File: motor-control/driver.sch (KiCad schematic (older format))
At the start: 24 parts

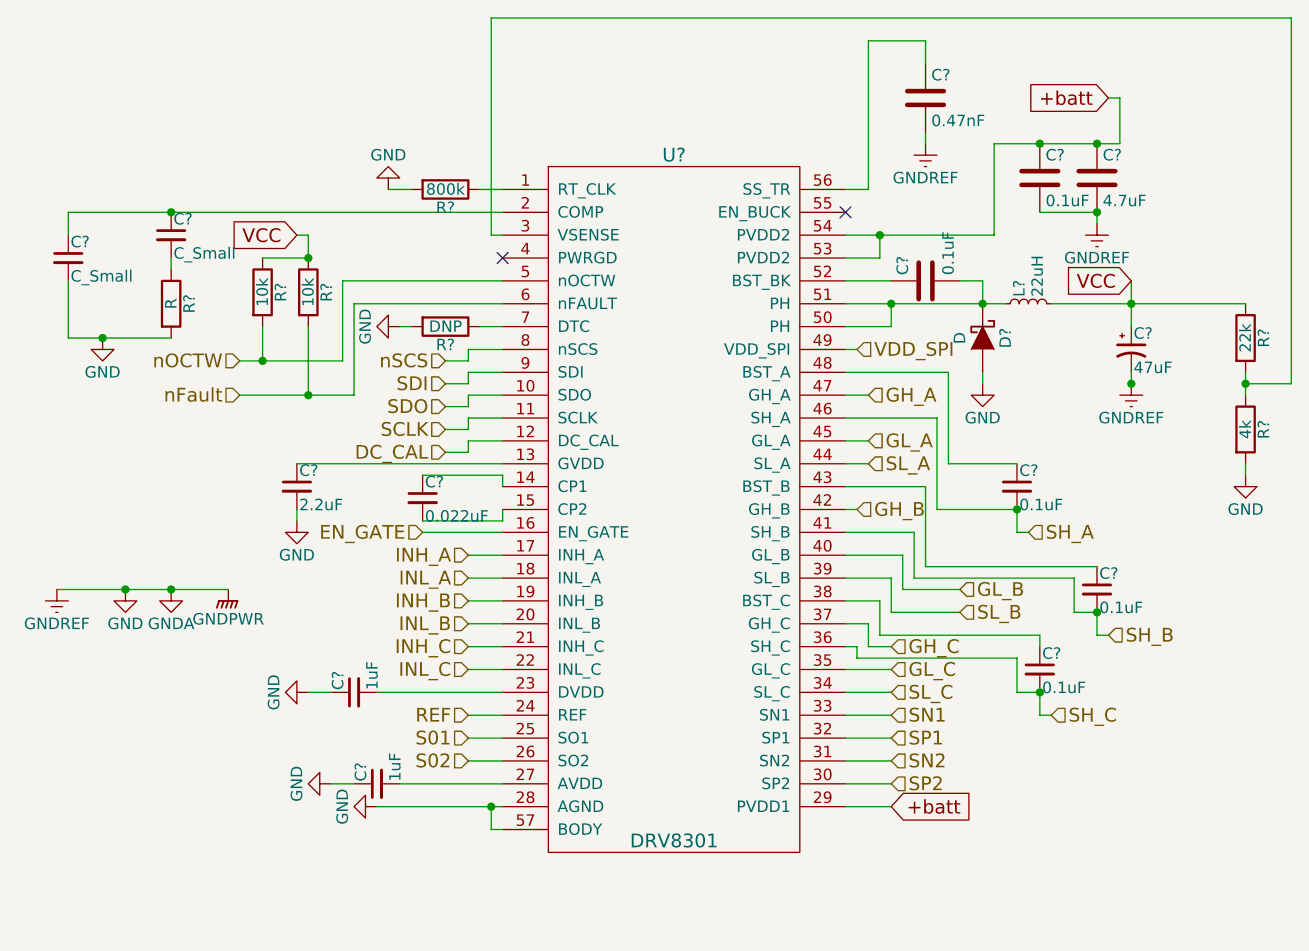
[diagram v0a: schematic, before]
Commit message: Annotated schematic & matched footprints
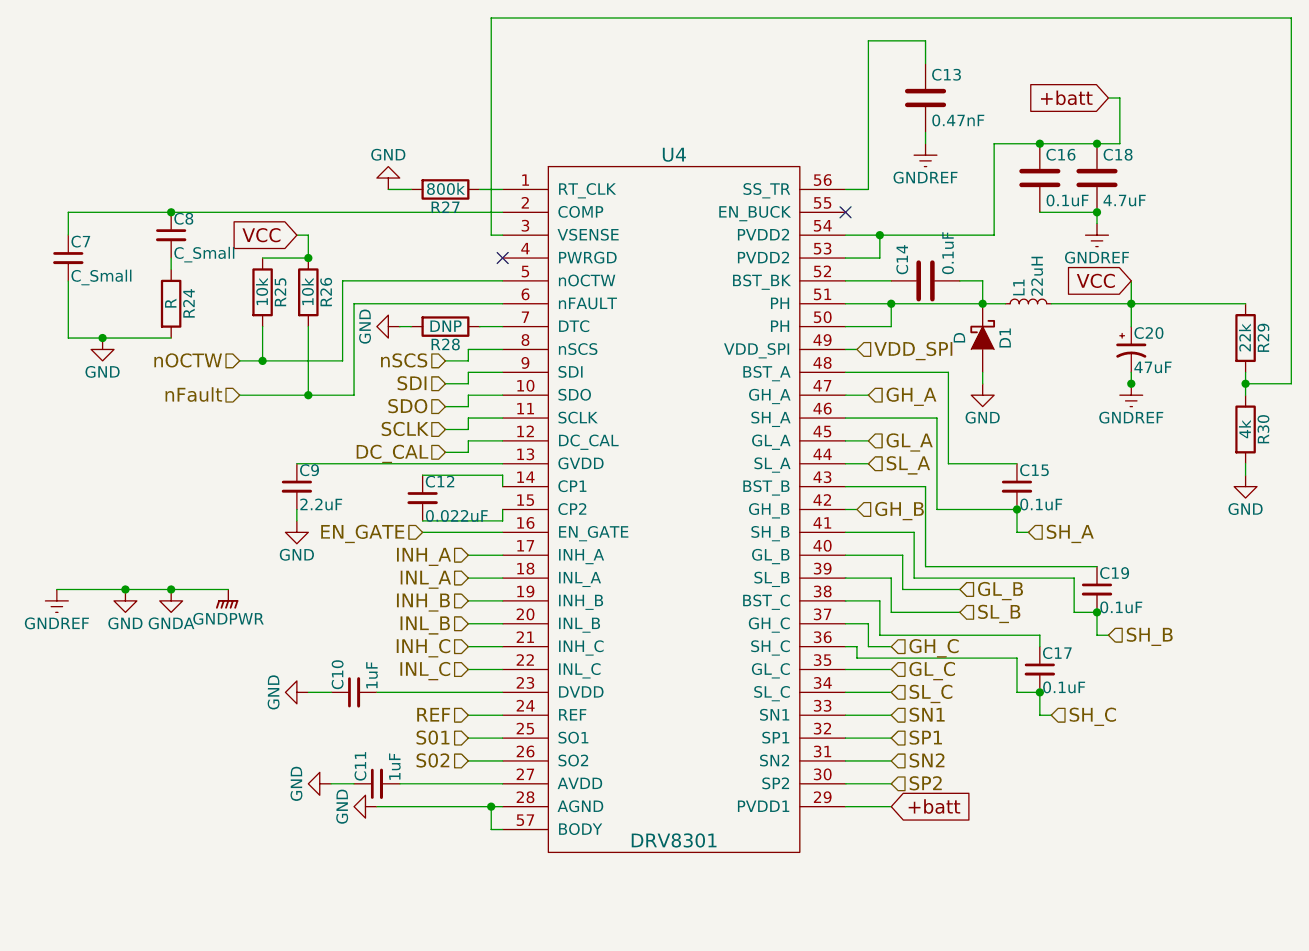
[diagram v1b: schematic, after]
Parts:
- C10, C11, C12, C13, C14, C15, C17, C19, C7, C8, C9: renamed from C?; footprint (none) -> Capacitors_SMD:C_0805
- C16: renamed from C?; footprint (none) -> Capacitors_Elko_ThroughHole:Elko_vert_31.5x14mm_RM5
- C18, C20: renamed from C?; footprint (none) -> Capacitors_Elko_ThroughHole:Elko_vert_31.5x16mm_RM7.5
- D1: renamed from D?; footprint (none) -> Capacitors_SMD:C_0805
- L1: renamed from L?; footprint (none) -> Capacitors_SMD:C_0805
- R24, R25, R26, R27, R28, R29, R30: renamed from R?; footprint (none) -> Resistors_SMD:R_0805
- U4: renamed from U?; footprint (none) -> p16261:DRV8301

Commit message: Just trying to get things together
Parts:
- C16: footprint Capacitors_Elko_ThroughHole:Elko_vert_31.5x14mm_RM5 -> Capacitors_SMD:C_0805
- C18, C20: footprint Capacitors_Elko_ThroughHole:Elko_vert_31.5x16mm_RM7.5 -> Capacitors_SMD:C_0805
- D1: footprint Capacitors_SMD:C_0805 -> Diodes_ThroughHole:Diode_TO-247_Vertical
- L1: footprint Capacitors_SMD:C_0805 -> Inductors:INDUCTOR_V
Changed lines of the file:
@@
 F 0 "C16" H 6525 2000 50  0000 L CNN
 F 1 "0.1uF" H 6525 1800 50  0000 L CNN
-F 2 "Capacitors_Elko_ThroughHole:Elko_vert_31.5x14mm_RM5" H 6538 1750 30  0001 C CNN
+F 2 "Capacitors_SMD:C_0805" H 6538 1750 30  0001 C CNN
 F 3 "" H 6500 1900 60  0000 C CNN
 	1    6500 1900
@@
 F 0 "C18" H 6775 2000 50  0000 L CNN
 F 1 "4.7uF" H 6775 1800 50  0000 L CNN
-F 2 "Capacitors_Elko_ThroughHole:Elko_vert_31.5x16mm_RM7.5" H 6788 1750 30  0001 C CNN
+F 2 "Capacitors_SMD:C_0805" H 6788 1750 30  0001 C CNN
 F 3 "" H 6750 1900 60  0000 C CNN
 	1    6750 1900
@@
 F 0 "L1" H 6480 2490 50  0000 L CNN
 F 1 "22uH" H 6480 2410 50  0000 L CNN
-F 2 "Capacitors_SMD:C_0805" H 6450 2450 60  0001 C CNN
+F 2 "Inductors:INDUCTOR_V" H 6450 2450 60  0001 C CNN
 F 3 "" H 6450 2450 60  0000 C CNN
 	1    6450 2450
@@
 F 0 "D1" H 6250 2700 50  0000 C CNN
 F 1 "D" H 6250 2500 50  0000 C CNN
-F 2 "Capacitors_SMD:C_0805" H 6250 2600 60  0001 C CNN
+F 2 "Diodes_ThroughHole:Diode_TO-247_Vertical" H 6250 2600 60  0001 C CNN
 F 3 "" H 6250 2600 60  0000 C CNN
 	1    6250 2600
@@
 F 0 "C20" H 6910 2720 50  0000 L CNN
 F 1 "47uF" H 6910 2570 50  0000 L CNN
-F 2 "Capacitors_Elko_ThroughHole:Elko_vert_31.5x16mm_RM7.5" H 6900 2650 60  0001 C CNN
+F 2 "Capacitors_SMD:C_0805" H 6900 2650 60  0001 C CNN
 F 3 "" H 6900 2650 60  0000 C CNN
 	1    6900 2650

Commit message: More changes
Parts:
- added C21: C_Small, symbol C_Small
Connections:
- net +batt: now also C21.1
- net GND: now also C21.2
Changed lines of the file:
@@
 $EndComp
 $Comp
-L GNDREF #PWR31
+L GNDREF #PWR32
 U 1 1 56449729
 P 6000 1750
-F 0 "#PWR31" H 6000 1500 50  0001 C CNN
+F 0 "#PWR32" H 6000 1500 50  0001 C CNN
 F 1 "GNDREF" H 6000 1600 50  0000 C CNN
 F 2 "" H 6000 1750 60  0000 C CNN
@@
 $EndComp
 $Comp
-L GNDREF #PWR33
+L GNDREF #PWR34
 U 1 1 5644A61D
 P 6750 2100
-F 0 "#PWR33" H 6750 1850 50  0001 C CNN
+F 0 "#PWR34" H 6750 1850 50  0001 C CNN
 F 1 "GNDREF" H 6750 1950 50  0000 C CNN
 F 2 "" H 6750 2100 60  0000 C CNN
@@
 VCC
 $Comp
-L GNDREF #PWR34
+L GNDREF #PWR35
 U 1 1 5644A955
 P 6900 2800
-F 0 "#PWR34" H 6900 2550 50  0001 C CNN
+F 0 "#PWR35" H 6900 2550 50  0001 C CNN
 F 1 "GNDREF" H 6900 2650 50  0000 C CNN
 F 2 "" H 6900 2800 60  0000 C CNN
@@
 	7400 2750 7400 2850
 $Comp
-L GND #PWR35
+L GND #PWR36
 U 1 1 56511C27
 P 7400 3200
-F 0 "#PWR35" H 7400 2950 50  0001 C CNN
+F 0 "#PWR36" H 7400 2950 50  0001 C CNN
 F 1 "GND" H 7400 3050 50  0000 C CNN
 F 2 "" H 7400 3200 60  0000 C CNN
@@
 Connection ~ 7400 2800
 $Comp
-L GND #PWR32
+L GND #PWR33
 U 1 1 56512446
 P 6250 2800
-F 0 "#PWR32" H 6250 2550 50  0001 C CNN
+F 0 "#PWR33" H 6250 2550 50  0001 C CNN
 F 1 "GND" H 6250 2650 50  0000 C CNN
 F 2 "" H 6250 2800 60  0000 C CNN
@@
 Connection ~ 2500 3700
 Connection ~ 2700 3700
+$Comp
+L C_Small C21
+U 1 1 56914993
+P 5700 4800
+F 0 "C21" H 5710 4870 50  0000 L CNN
+F 1 "C_Small" H 5710 4720 50  0000 L CNN
+F 2 "" H 5700 4800 50  0000 C CNN
+F 3 "" H 5700 4800 50  0000 C CNN
+	1    5700 4800
+	1    0    0    -1
+$EndComp
+$Comp
+L GND #PWR31
+U 1 1 56914B46
+P 5700 5000
+F 0 "#PWR31" H 5700 4750 50  0001 C CNN
+F 1 "GND" H 5700 4850 50  0000 C CNN
+F 2 "" H 5700 5000 50  0000 C CNN
+F 3 "" H 5700 5000 50  0000 C CNN
+	1    5700 5000
+	1    0    0    -1
+$EndComp
+Wire Wire Line
+	5700 4900 5700 5000
+Wire Wire Line
+	5700 4700 5700 4650
+Connection ~ 5700 4650
 $EndSCHEMATC

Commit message: Stuff I didn't commit from last time
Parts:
- C21: footprint (none) -> Capacitors_SMD:C_0805
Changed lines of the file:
@@
 $EndComp
 $Comp
-L GNDREF #PWR32
+L GNDREF #PWR020
 U 1 1 56449729
 P 6000 1750
-F 0 "#PWR32" H 6000 1500 50  0001 C CNN
+F 0 "#PWR020" H 6000 1500 50  0001 C CNN
 F 1 "GNDREF" H 6000 1600 50  0000 C CNN
 F 2 "" H 6000 1750 60  0000 C CNN
@@
 $EndComp
 $Comp
-L GNDREF #PWR34
+L GNDREF #PWR021
 U 1 1 5644A61D
 P 6750 2100
-F 0 "#PWR34" H 6750 1850 50  0001 C CNN
+F 0 "#PWR021" H 6750 1850 50  0001 C CNN
 F 1 "GNDREF" H 6750 1950 50  0000 C CNN
 F 2 "" H 6750 2100 60  0000 C CNN
@@
 VCC
 $Comp
-L GNDREF #PWR35
+L GNDREF #PWR022
 U 1 1 5644A955
 P 6900 2800
-F 0 "#PWR35" H 6900 2550 50  0001 C CNN
+F 0 "#PWR022" H 6900 2550 50  0001 C CNN
 F 1 "GNDREF" H 6900 2650 50  0000 C CNN
 F 2 "" H 6900 2800 60  0000 C CNN
@@
 $EndComp
 $Comp
-L GND #PWR29
+L GND #PWR023
 U 1 1 5650F368
 P 3650 1950
-F 0 "#PWR29" H 3650 1700 50  0001 C CNN
+F 0 "#PWR023" H 3650 1700 50  0001 C CNN
 F 1 "GND" H 3650 1800 50  0000 C CNN
 F 2 "" H 3650 1950 60  0000 C CNN
@@
 	2250 2600 2700 2600
 $Comp
-L GND #PWR21
+L GND #PWR024
 U 1 1 5650F526
 P 2400 2600
-F 0 "#PWR21" H 2400 2350 50  0001 C CNN
+F 0 "#PWR024" H 2400 2350 50  0001 C CNN
 F 1 "GND" H 2400 2450 50  0000 C CNN
 F 2 "" H 2400 2600 60  0000 C CNN
@@
 $EndComp
 $Comp
-L GND #PWR26
+L GND #PWR025
 U 1 1 5650F58D
 P 3300 4150
-F 0 "#PWR26" H 3300 3900 50  0001 C CNN
+F 0 "#PWR025" H 3300 3900 50  0001 C CNN
 F 1 "GND" H 3300 4000 50  0000 C CNN
 F 2 "" H 3300 4150 60  0000 C CNN
@@
 $EndComp
 $Comp
-L GND #PWR27
+L GND #PWR026
 U 1 1 5650FDA1
 P 3400 4550
-F 0 "#PWR27" H 3400 4300 50  0001 C CNN
+F 0 "#PWR026" H 3400 4300 50  0001 C CNN
 F 1 "GND" H 3400 4400 50  0000 C CNN
 F 2 "" H 3400 4550 60  0000 C CNN
@@
 	3700 4550 4150 4550
 $Comp
-L GND #PWR28
+L GND #PWR027
 U 1 1 5650FE56
 P 3600 4650
-F 0 "#PWR28" H 3600 4400 50  0001 C CNN
+F 0 "#PWR027" H 3600 4400 50  0001 C CNN
 F 1 "GND" H 3600 4500 50  0000 C CNN
 F 2 "" H 3600 4650 60  0000 C CNN
@@
 	7400 2750 7400 2850
 $Comp
-L GND #PWR36
+L GND #PWR028
 U 1 1 56511C27
 P 7400 3200
-F 0 "#PWR36" H 7400 2950 50  0001 C CNN
+F 0 "#PWR028" H 7400 2950 50  0001 C CNN
 F 1 "GND" H 7400 3050 50  0000 C CNN
 F 2 "" H 7400 3200 60  0000 C CNN
@@
 Connection ~ 7400 2800
 $Comp
-L GND #PWR33
+L GND #PWR029
 U 1 1 56512446
 P 6250 2800
-F 0 "#PWR33" H 6250 2550 50  0001 C CNN
+F 0 "#PWR029" H 6250 2550 50  0001 C CNN
 F 1 "GND" H 6250 2650 50  0000 C CNN
 F 2 "" H 6250 2800 60  0000 C CNN
@@
 $EndComp
 $Comp
-L GND #PWR30
+L GND #PWR030
 U 1 1 56513ADE
 P 3700 2550
-F 0 "#PWR30" H 3700 2300 50  0001 C CNN
+F 0 "#PWR030" H 3700 2300 50  0001 C CNN
 F 1 "GND" H 3700 2400 50  0000 C CNN
 F 2 "" H 3700 2550 60  0000 C CNN
@@
 	4000 3050 4150 3050
 $Comp
-L GND #PWR25
+L GND #PWR031
 U 1 1 565164C8
 P 3250 3400
-F 0 "#PWR25" H 3250 3150 50  0001 C CNN
+F 0 "#PWR031" H 3250 3150 50  0001 C CNN
 F 1 "GND" H 3250 3250 50  0000 C CNN
 F 2 "" H 3250 3400 60  0000 C CNN
@@
 	5650 4250 5850 4250
 $Comp
-L GND #PWR22
+L GND #PWR032
 U 1 1 5651CA8A
 P 2500 3700
-F 0 "#PWR22" H 2500 3450 50  0001 C CNN
+F 0 "#PWR032" H 2500 3450 50  0001 C CNN
 F 1 "GND" H 2500 3550 50  0000 C CNN
 F 2 "" H 2500 3700 60  0000 C CNN
@@
 $EndComp
 $Comp
-L GNDA #PWR23
+L GNDA #PWR033
 U 1 1 5651CACE
 P 2700 3700
-F 0 "#PWR23" H 2700 3450 50  0001 C CNN
+F 0 "#PWR033" H 2700 3450 50  0001 C CNN
 F 1 "GNDA" H 2700 3550 50  0000 C CNN
 F 2 "" H 2700 3700 60  0000 C CNN
@@
 $EndComp
 $Comp
-L GNDPWR #PWR24
+L GNDPWR #PWR034
 U 1 1 5651CB12
 P 2950 3700
-F 0 "#PWR24" H 2950 3500 50  0001 C CNN
+F 0 "#PWR034" H 2950 3500 50  0001 C CNN
 F 1 "GNDPWR" H 2950 3570 50  0000 C CNN
 F 2 "" H 2950 3650 60  0000 C CNN
@@
 $EndComp
 $Comp
-L GNDREF #PWR20
+L GNDREF #PWR035
 U 1 1 5651CB56
 P 2200 3700
-F 0 "#PWR20" H 2200 3450 50  0001 C CNN
+F 0 "#PWR035" H 2200 3450 50  0001 C CNN
 F 1 "GNDREF" H 2200 3550 50  0000 C CNN
 F 2 "" H 2200 3700 60  0000 C CNN
@@
 F 0 "C21" H 5710 4870 50  0000 L CNN
 F 1 "C_Small" H 5710 4720 50  0000 L CNN
-F 2 "" H 5700 4800 50  0000 C CNN
+F 2 "Capacitors_SMD:C_0805" H 5700 4800 50  0001 C CNN
 F 3 "" H 5700 4800 50  0000 C CNN
 	1    5700 4800
@@
 $EndComp
 $Comp
-L GND #PWR31
+L GND #PWR036
 U 1 1 56914B46
 P 5700 5000
-F 0 "#PWR31" H 5700 4750 50  0001 C CNN
+F 0 "#PWR036" H 5700 4750 50  0001 C CNN
 F 1 "GND" H 5700 4850 50  0000 C CNN
 F 2 "" H 5700 5000 50  0000 C CNN

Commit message: Modified Schematic Comp resist/cap vals, added bom
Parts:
- R28: value DNP -> 0R
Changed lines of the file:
@@
 P 3900 2550
 F 0 "R28" V 3980 2550 50  0000 C CNN
-F 1 "DNP" V 3900 2550 50  0000 C CNN
+F 1 "0R" V 3900 2550 50  0000 C CNN
 F 2 "Resistors_SMD:R_0805" V 3830 2550 30  0001 C CNN
 F 3 "" H 3900 2550 30  0000 C CNN

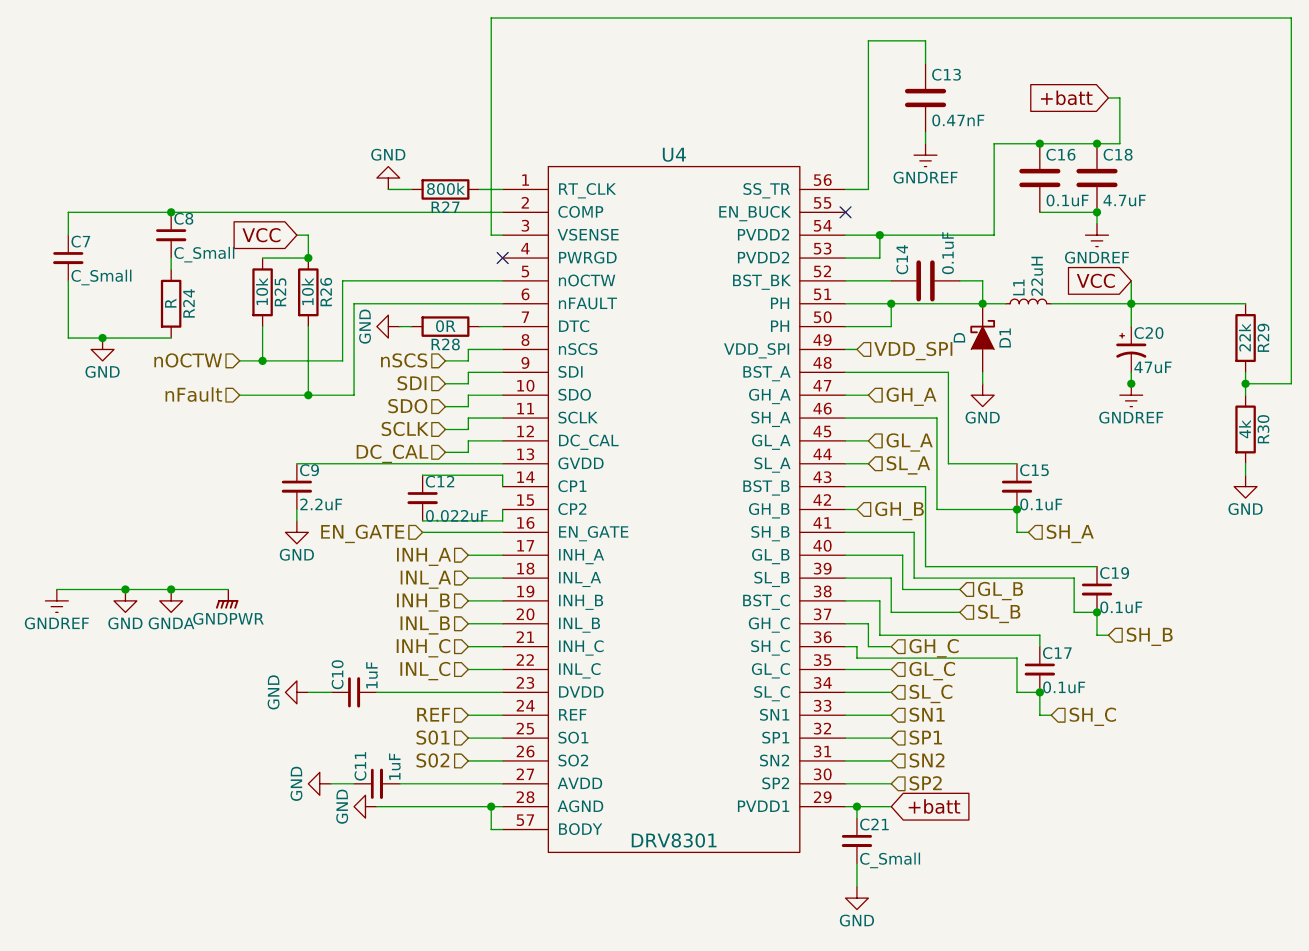
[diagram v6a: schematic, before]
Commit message: Added some datasheet links, additional RC values
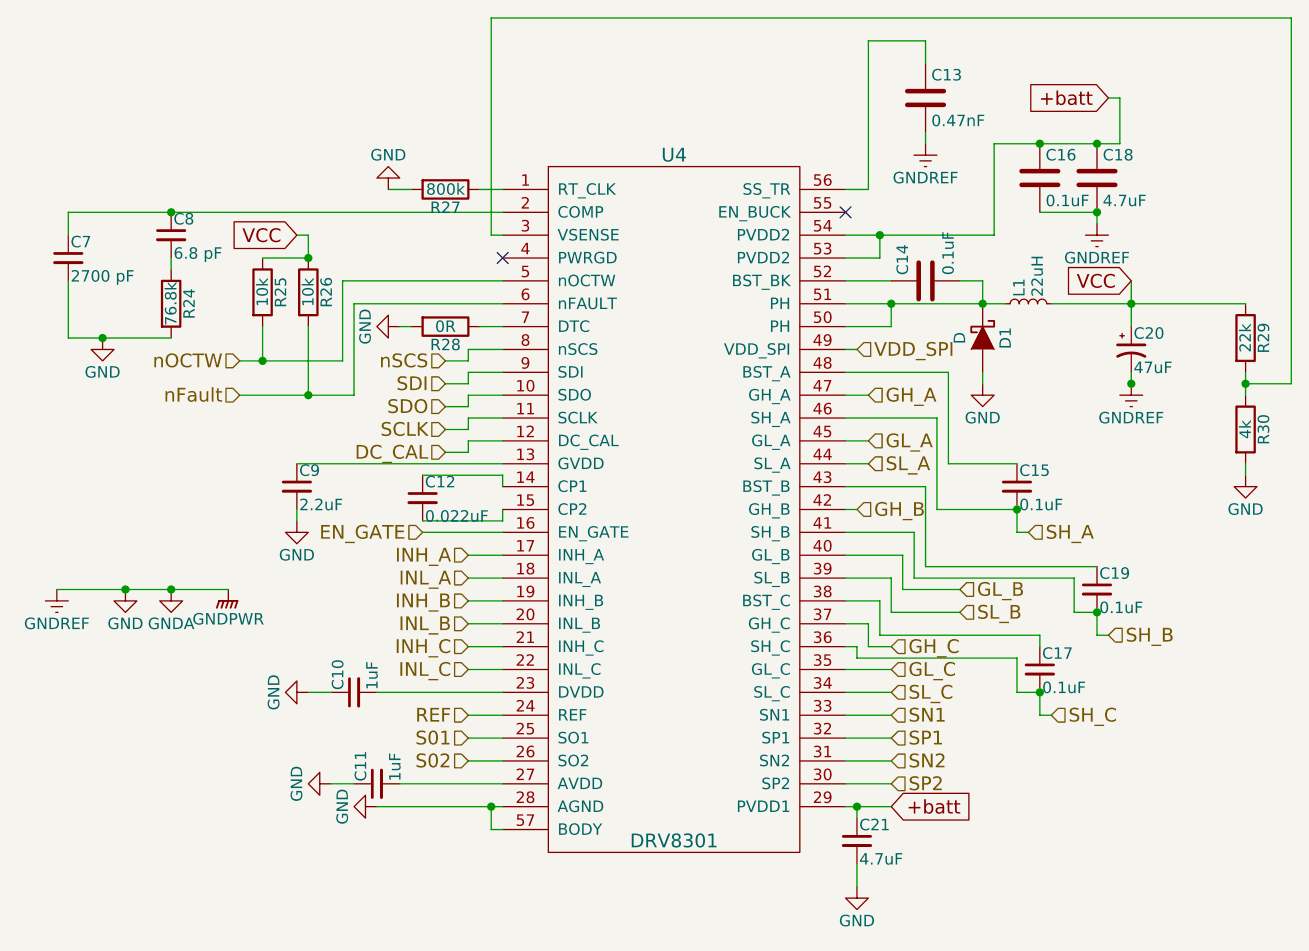
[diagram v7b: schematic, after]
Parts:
- C10, C20: Voltage (none) -> 6.3 V
- C11, C14: Voltage (none) -> 10 V
- C15, C17, C19, C9: Voltage (none) -> 16 V
- C16, C18: Voltage (none) -> 100 V
- C21: value C_Small -> 4.7uF; Voltage (none) -> 100 V
- C7: value C_Small -> 2700 pF
- C8: value C_Small -> 6.8 pF
- R24: value R -> 76.8k
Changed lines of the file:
@@
 F 2 "Capacitors_SMD:C_0805" H 6538 1750 30  0001 C CNN
 F 3 "" H 6500 1900 60  0000 C CNN
+F 4 "100 V" H 6500 1900 60  0001 C CNN "Voltage"
 	1    6500 1900
 	1    0    0    -1
@@
 F 2 "Capacitors_SMD:C_0805" H 6788 1750 30  0001 C CNN
 F 3 "" H 6750 1900 60  0000 C CNN
+F 4 "100 V" H 6750 1900 60  0001 C CNN "Voltage"
 	1    6750 1900
 	1    0    0    -1
@@
 F 2 "Capacitors_SMD:C_0805" H 6038 2200 30  0001 C CNN
 F 3 "" H 6000 2350 60  0000 C CNN
+F 4 "10 V" H 6000 2350 60  0001 C CNN "Voltage"
 	1    6000 2350
 	0    -1   -1   0
@@
 F 2 "Capacitors_SMD:C_0805" H 6900 2650 60  0001 C CNN
 F 3 "" H 6900 2650 60  0000 C CNN
+F 4 "6.3 V" H 6900 2650 60  0001 C CNN "Voltage"
 	1    6900 2650
 	1    0    0    -1
@@
 F 2 "Capacitors_SMD:C_0805" H 3250 3250 60  0001 C CNN
 F 3 "" H 3250 3250 60  0000 C CNN
+F 4 "16 V" H 3250 3250 60  0001 C CNN "Voltage"
 	1    3250 3250
 	1    0    0    -1
@@
 P 2250 2250
 F 0 "C7" H 2260 2320 50  0000 L CNN
-F 1 "C_Small" H 2260 2170 50  0000 L CNN
+F 1 "2700 pF" H 2260 2170 50  0000 L CNN
 F 2 "Capacitors_SMD:C_0805" H 2250 2250 60  0001 C CNN
 F 3 "" H 2250 2250 60  0000 C CNN
@@
 P 2700 2150
 F 0 "C8" H 2710 2220 50  0000 L CNN
-F 1 "C_Small" H 2710 2070 50  0000 L CNN
+F 1 "6.8 pF" H 2710 2070 50  0000 L CNN
 F 2 "Capacitors_SMD:C_0805" H 2700 2150 60  0001 C CNN
 F 3 "" H 2700 2150 60  0000 C CNN
@@
 P 2700 2450
 F 0 "R24" V 2780 2450 50  0000 C CNN
-F 1 "R" V 2700 2450 50  0000 C CNN
+F 1 "76.8k" V 2700 2450 50  0000 C CNN
 F 2 "Resistors_SMD:R_0805" V 2630 2450 30  0001 C CNN
 F 3 "" H 2700 2450 30  0000 C CNN
@@
 F 2 "Capacitors_SMD:C_0805" H 3500 4150 60  0001 C CNN
 F 3 "" H 3500 4150 60  0000 C CNN
+F 4 "6.3 V" H 3500 4150 60  0001 C CNN "Voltage"
 	1    3500 4150
 	0    -1   -1   0
@@
 F 2 "Capacitors_SMD:C_0805" H 3600 4550 60  0001 C CNN
 F 3 "" H 3600 4550 60  0000 C CNN
+F 4 "10 V" H 3600 4550 60  0001 C CNN "Voltage"
 	1    3600 4550
 	0    -1   -1   0
@@
 F 2 "Capacitors_SMD:C_0805" H 6400 3250 60  0001 C CNN
 F 3 "" H 6400 3250 60  0000 C CNN
+F 4 "16 V" H 6400 3250 60  0001 C CNN "Voltage"
 	1    6400 3250
 	1    0    0    -1
@@
 F 2 "Capacitors_SMD:C_0805" H 6750 3700 60  0001 C CNN
 F 3 "" H 6750 3700 60  0000 C CNN
+F 4 "16 V" H 6750 3700 60  0001 C CNN "Voltage"
 	1    6750 3700
 	1    0    0    -1
@@
 F 2 "Capacitors_SMD:C_0805" H 6500 4050 60  0001 C CNN
 F 3 "" H 6500 4050 60  0000 C CNN
+F 4 "16 V" H 6500 4050 60  0001 C CNN "Voltage"
 	1    6500 4050
 	1    0    0    -1
@@
 P 5700 4800
 F 0 "C21" H 5710 4870 50  0000 L CNN
-F 1 "C_Small" H 5710 4720 50  0000 L CNN
+F 1 "4.7uF" H 5710 4720 50  0000 L CNN
 F 2 "Capacitors_SMD:C_0805" H 5700 4800 50  0001 C CNN
 F 3 "" H 5700 4800 50  0000 C CNN
+F 4 "100 V" H 5700 4800 60  0001 C CNN "Voltage"
 	1    5700 4800
 	1    0    0    -1
